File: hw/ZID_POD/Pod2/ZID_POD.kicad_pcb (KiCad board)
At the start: 2 copper layers, 52.8 x 19.3 mm, 2 parts, among them J1 Z80-POD

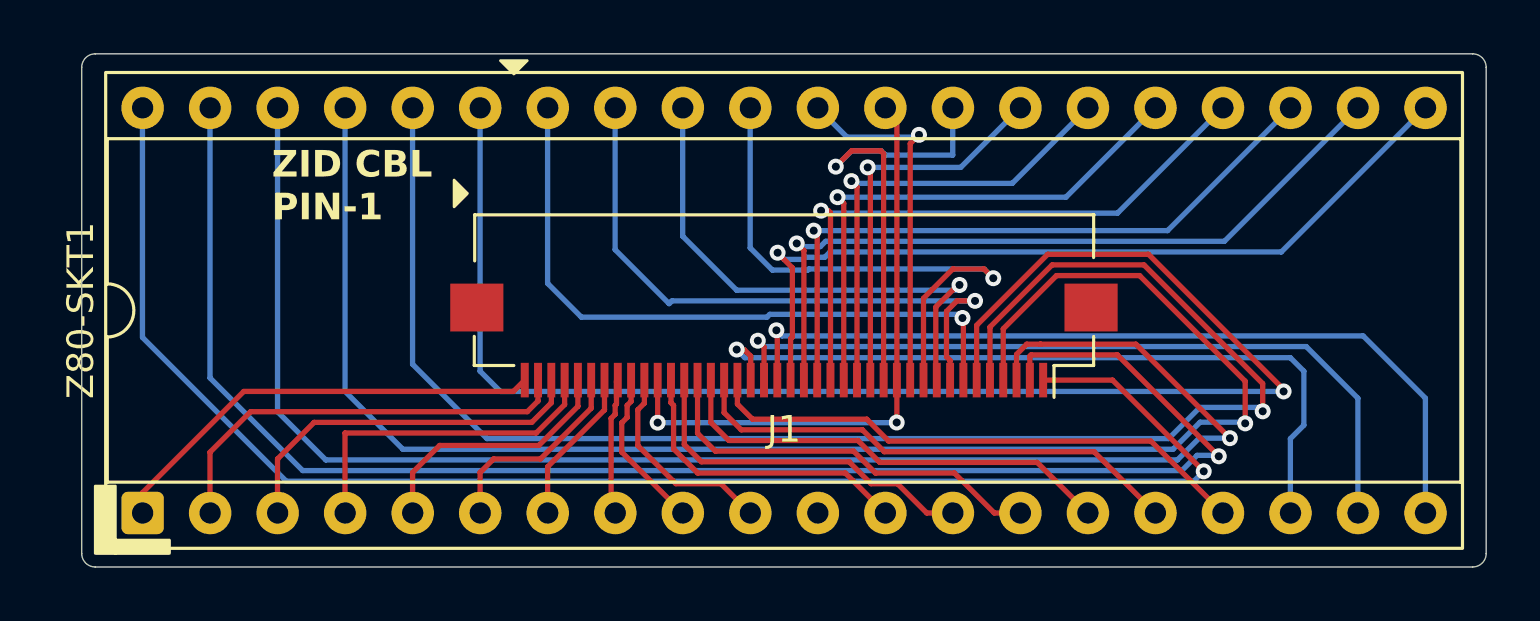
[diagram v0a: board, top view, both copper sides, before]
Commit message: POD PCB increase GND trace width
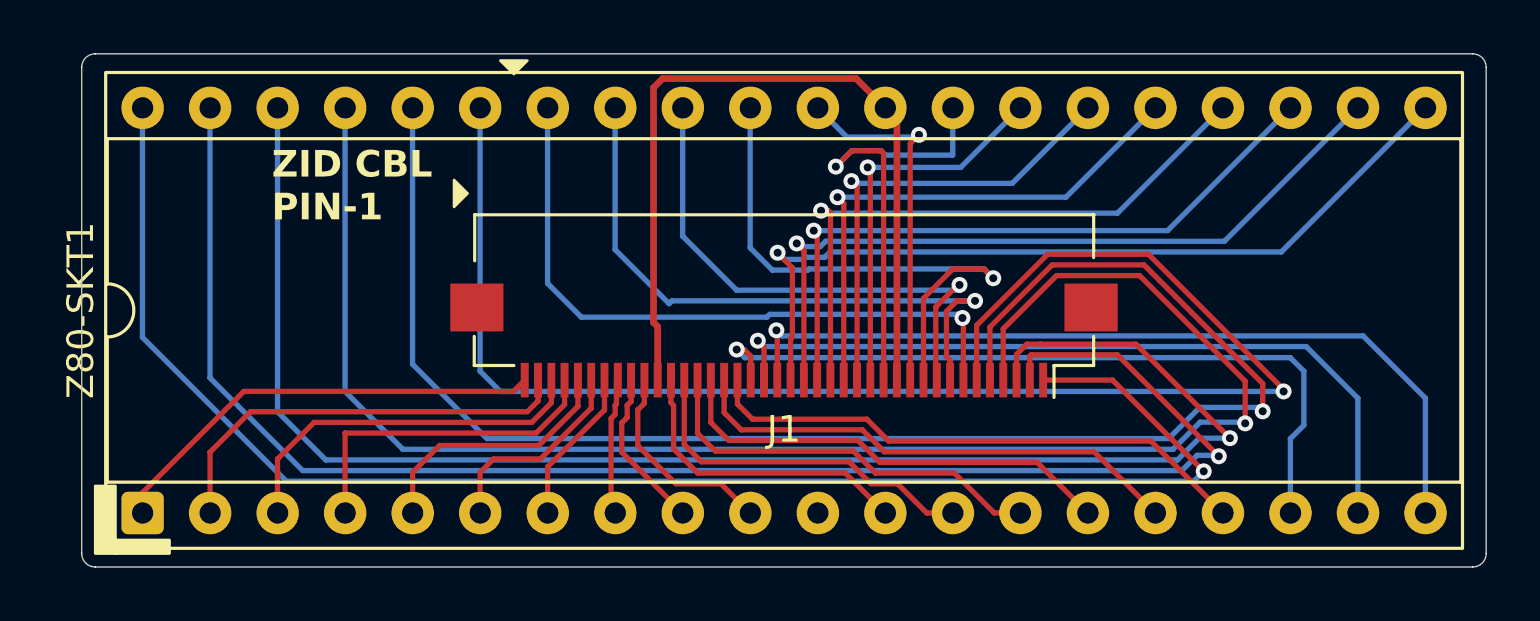
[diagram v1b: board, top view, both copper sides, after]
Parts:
- J1: value Z80-POD -> Z80-POD (2)
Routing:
- net /GND: track 22.0 -> 30.2 mm, vias 2 -> 0
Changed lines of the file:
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@@
 	)
 	(setup
+		(stackup
+			(layer "F.SilkS"
+				(type "Top Silk Screen")
+			)
+			(layer "F.Paste"
+				(type "Top Solder Paste")
+			)
+			(layer "F.Mask"
+				(type "Top Solder Mask")
+				(thickness 0.01)
+			)
+			(layer "F.Cu"
+				(type "copper")
+				(thickness 0.035)
+			)
+			(layer "dielectric 1"
+				(type "core")
+				(thickness 1.51)
+				(material "FR4")
+				(epsilon_r 4.5)
+				(loss_tangent 0.02)
+			)
+			(layer "B.Cu"
+				(type "copper")
+				(thickness 0.035)
+			)
+			(layer "B.Mask"
+				(type "Bottom Solder Mask")
+				(thickness 0.01)
+			)
+			(layer "B.Paste"
+				(type "Bottom Solder Paste")
+			)
+			(layer "B.SilkS"
+				(type "Bottom Silk Screen")
+			)
+			(copper_finish "None")
+			(dielectric_constraints no)
+		)
 		(pad_to_mask_clearance 0)
 		(allow_soldermask_bridges_in_footprints no)
@@
 			)
 		)
-		(property "Value" "Z80-POD"
+		(property "Value" "Z80-POD (2)"
 			(at 0 5.6 0)
 			(layer "B.SilkS")
@@
 	)
 	(segment
-		(start 120.582 106.0622)
-		(end 120.5738 106.0704)
-		(width 0.2)
+		(start 111.7688 93.133)
+		(end 111.426 93.4758)
+		(width 0.254)
 		(layer "F.Cu")
 		(net 3)
 	)
 	(segment
-		(start 111.582 104.476201)
-		(end 111.582 106.0752)
-		(width 0.2)
+		(start 111.582 102.4634)
+		(end 111.582 104.476201)
+		(width 0.254)
 		(layer "F.Cu")
 		(net 3)
 	)
 	(segment
-		(start 111.582 106.0752)
-		(end 111.581 106.0762)
-		(width 0.2)
+		(start 111.426 93.4758)
+		(end 111.426 102.3074)
+		(width 0.254)
 		(layer "F.Cu")
 		(net 3)
 	)
 	(segment
-		(start 120.582 104.476201)
-		(end 120.582 106.0622)
-		(width 0.2)
+		(start 119.046 93.133)
+		(end 111.7688 93.133)
+		(width 0.254)
+		(layer "F.Cu")
+		(net 3)
+	)
+	(segment
+		(start 120.147 94.234)
+		(end 119.046 93.133)
+		(width 0.254)
 		(layer "F.Cu")
 		(net 3)
@@
 		(start 120.582 104.476201)
 		(end 120.582 94.674)
-		(width 0.2)
+		(width 0.254)
 		(layer "F.Cu")
 		(net 3)
 	)
-	(via
-		(at 111.581 106.0762)
-		(size 0.6)
-		(drill 0.3)
-		(layers "F.Cu" "B.Cu")
+	(segment
+		(start 111.426 102.3074)
+		(end 111.582 102.4634)
+		(width 0.254)
+		(layer "F.Cu")
 		(net 3)
 	)
-	(via
-		(at 120.5738 106.0704)
-		(size 0.6)
-		(drill 0.3)
-		(layers "F.Cu" "B.Cu")
-		(net 3)
-	)
-	(segment
-		(start 120.5738 106.0704)
-		(end 120.568 106.0762)
-		(width 0.2)
-		(layer "B.Cu")
-		(net 3)
-	)
-	(segment
-		(start 120.568 106.0762)
-		(end 111.581 106.0762)
-		(width 0.2)
-		(layer "B.Cu")
-		(net 3)
-	)
